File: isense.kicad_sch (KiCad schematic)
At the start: 29 parts, among them U2 OPA551U, U3 OPA551U, U4 TLV9301

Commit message: Update Mouser part numbers
Some resistors will be wrong, please check
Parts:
- U?: Mouser Part Number (none) -> 595-INA138NA/3K
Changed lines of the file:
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@@
+			)
+		)
+		(property "Mouser Part Number" "595-INA138NA/3K"
+			(at 44.45 41.91 0)
+			(effects
+				(font
+					(size 1.27 1.27)
+				)
+				(hide yes)
 			)
 		)

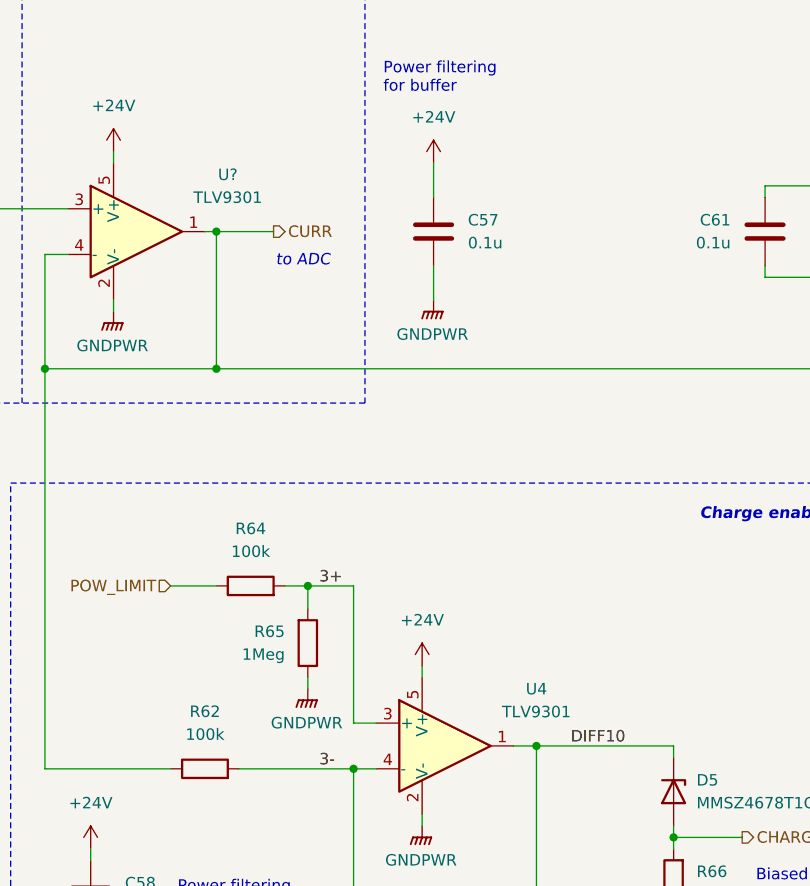
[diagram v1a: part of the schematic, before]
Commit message: Tuned circuits & adjusted values
Changed footprints for some circuits to consolidate components
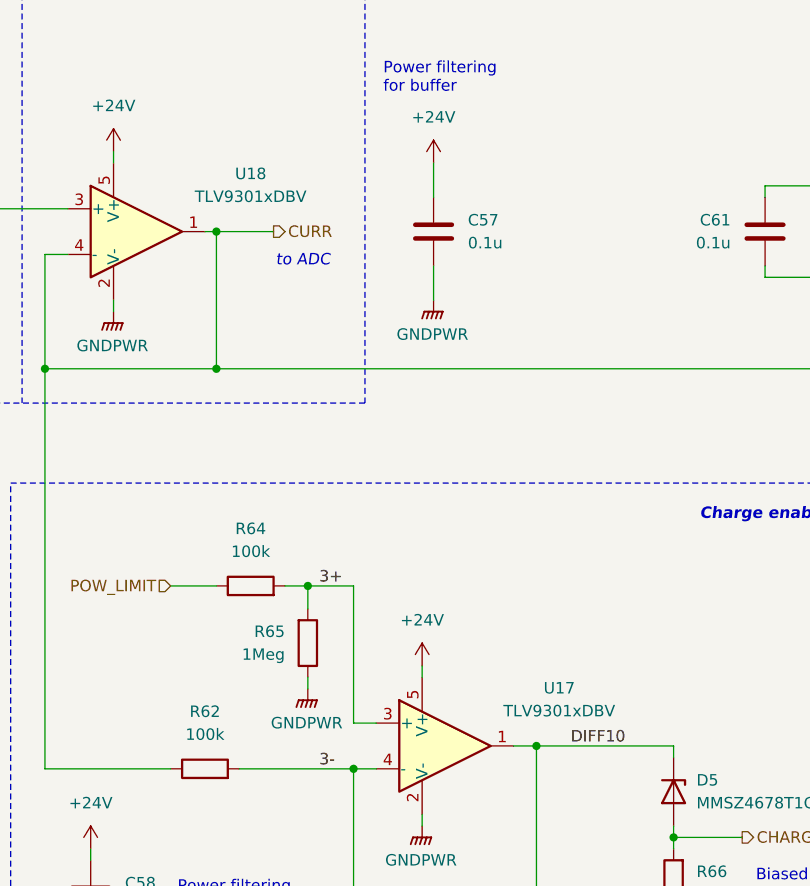
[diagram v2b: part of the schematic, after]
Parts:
- removed U4, U?: TLV9301, Package_TO_SOT_SMD:SOT-23-5_HandSoldering, symbol Amplifier_Operational:LM321
- added U17, U18: TLV9301xDBV, Package_TO_SOT_SMD:SOT-23-5_HandSoldering, symbol Amplifier_Operational:TLV9301xDBV
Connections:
- net +24V: now also U17.5 (V+), U18.5 (V+)
- net 3+: now also U17.3 (+)
- net 3-: now also U17.4 (-)
- net CURR: now also U18.1, U18.4 (-)
- net CURR_{RAW}: now also U18.3 (+)
- net DIFF10: now also U17.1
- net GNDPWR: now also U17.2 (V-), U18.2 (V-)

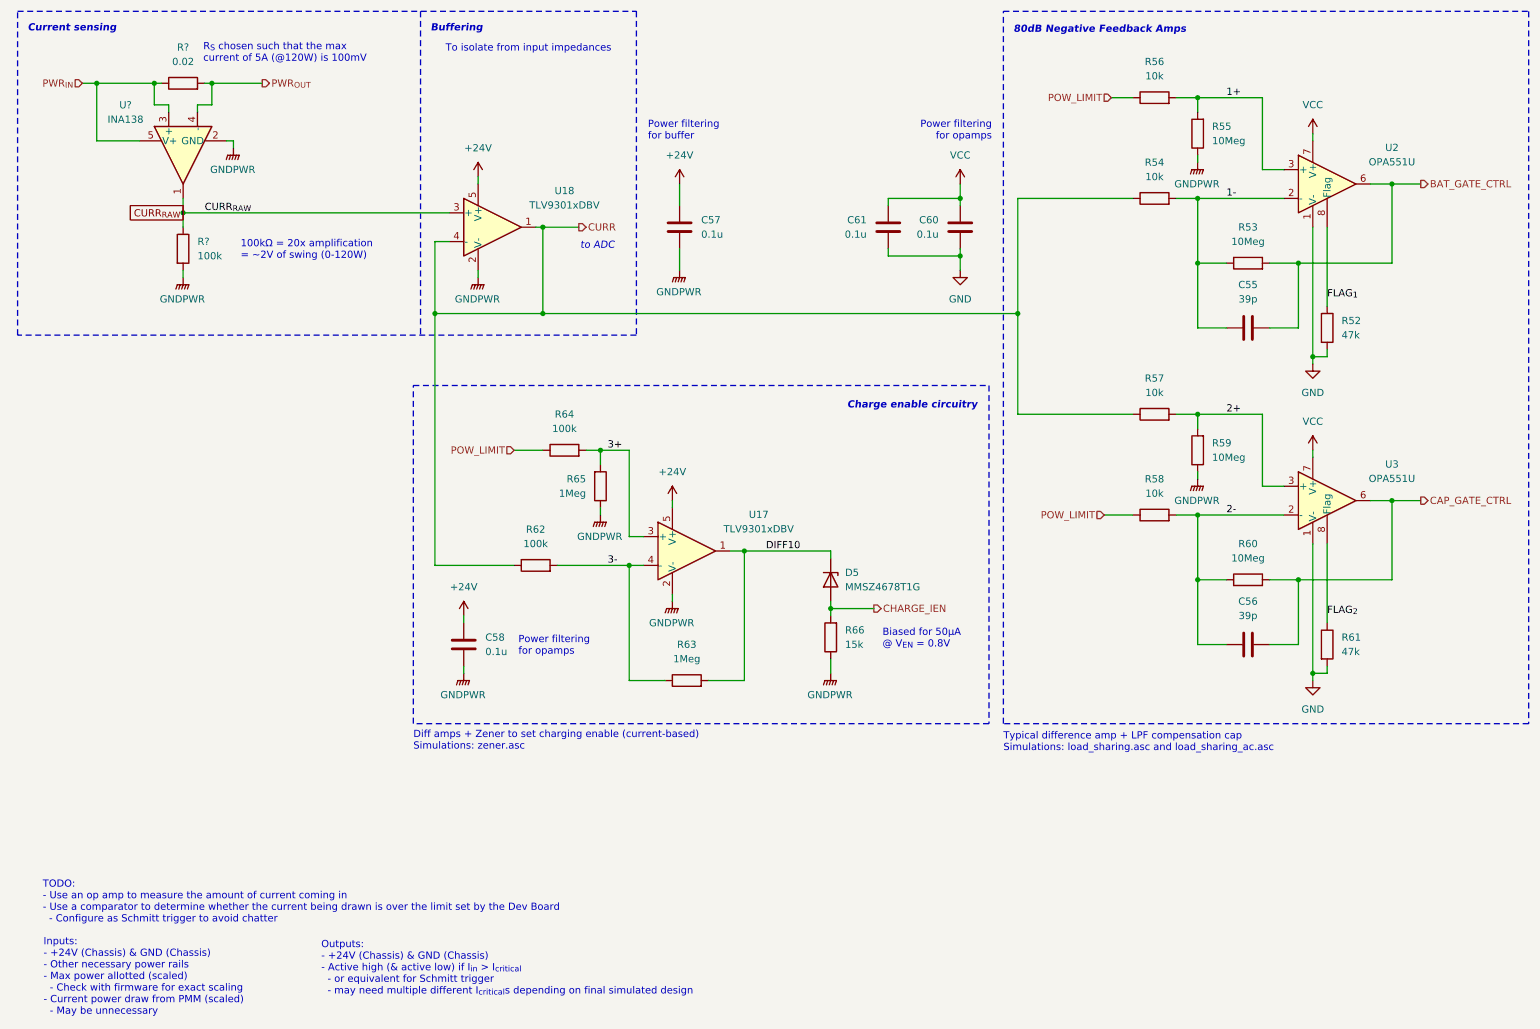
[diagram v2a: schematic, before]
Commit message: Transfer new design to schematic
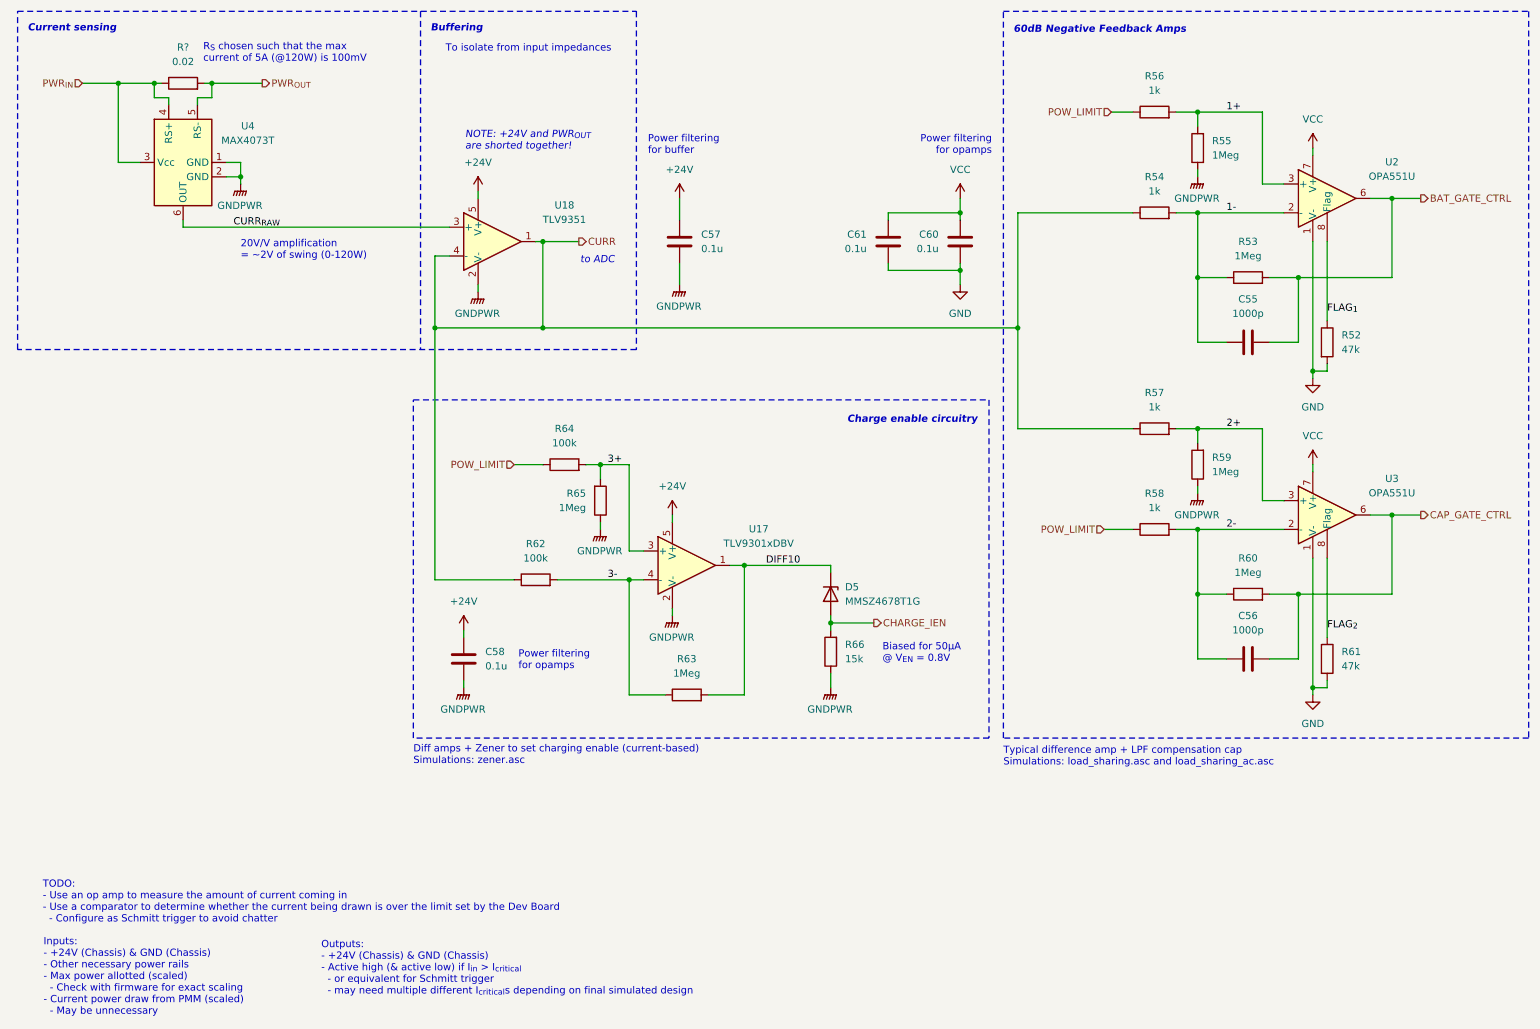
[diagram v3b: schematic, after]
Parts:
- removed R?: 100k, Resistor_SMD:R_0603_1608Metric_Pad0.98x0.95mm_HandSolder, symbol Device:R
- removed U?: INA138, Package_TO_SOT_SMD:SOT-23-5, symbol Amplifier_Current:INA138
- added U4: MAX4073T, Package_TO_SOT_SMD:SOT-23-6_Handsoldering, symbol Amplifier_Current:MAX4080T
- C55, C56: value 39p -> 1000p
- R53, R55, R59, R60: value 10Meg -> 1Meg
- R54, R56, R57, R58: value 10k -> 1k
- U18: value TLV9301xDBV -> TLV9351; Mouser Part Number 595-TLV9301IDBVR -> 595-TLV9351IDCKR
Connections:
- net CURR_{RAW}: now also U4.6 (OUT)
- net GNDPWR: now also U4.1 (GND), U4.2 (GND)
- net PWR_{IN}: now also U4.3 (Vcc), U4.4 (RS+)
- net PWR_{OUT}: now also U4.5 (RS-)
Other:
- note added: "20V/V amplification = ~2V of swing (0-120W)"
- note added: "60dB Negative Feedback Amps"
- note added: "NOTE: +24V and PWR_{OUT} are shorted together!"
- note removed: "100kΩ = 20x amplification = ~2V of swing (0-120W)"
- note removed: "80dB Negative Feedback Amps"
- moved on the sheet: C55, C56, C57, C58, C60, C61, D5, R52, R53, R54, R55, R56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

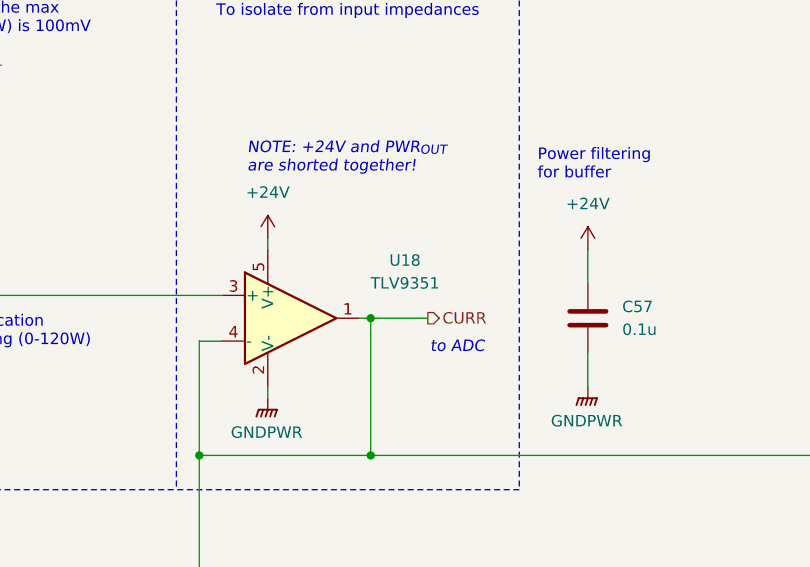
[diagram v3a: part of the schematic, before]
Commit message: Find suitable op-amp for buffer in current sense
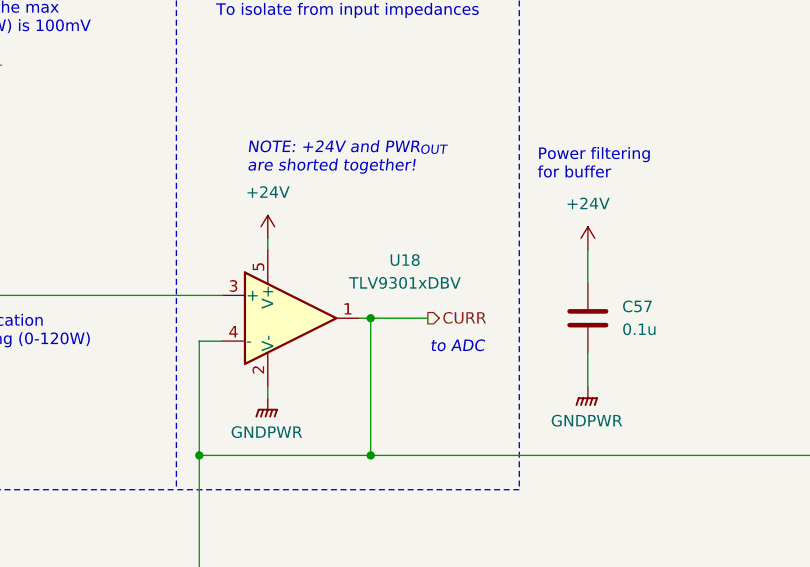
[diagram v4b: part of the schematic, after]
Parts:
- U18: value TLV9351 -> TLV9301xDBV; Mouser Part Number 595-TLV9351IDCKR -> 595-TLV9301IDBVR

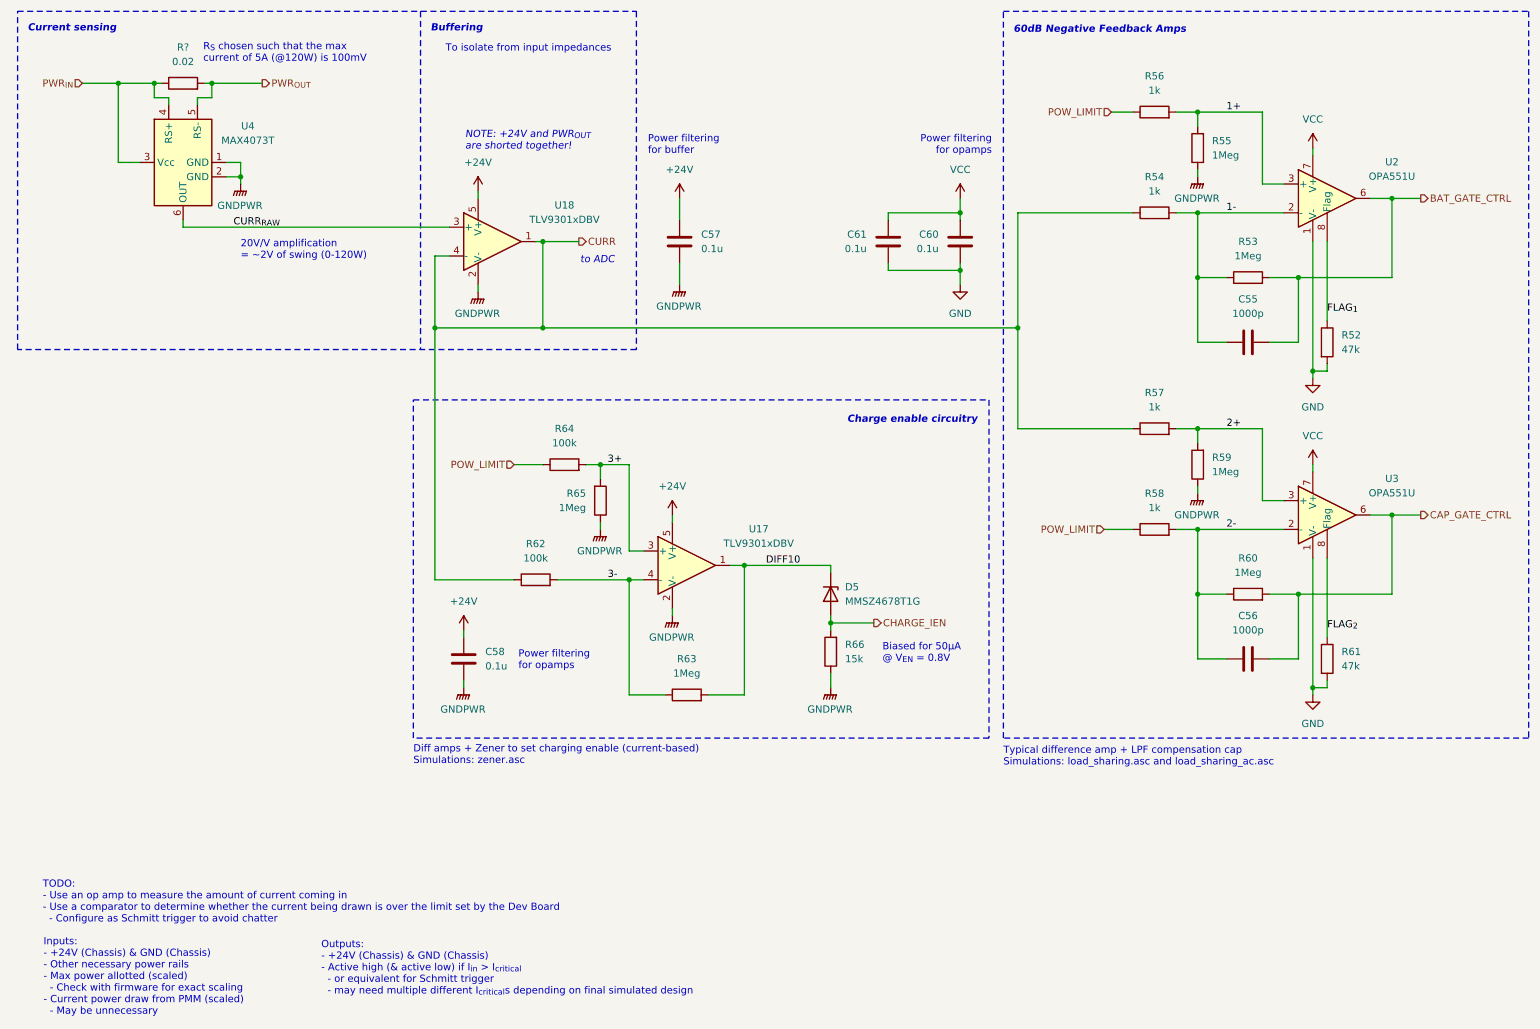
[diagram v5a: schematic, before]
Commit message: Reannotate schematic
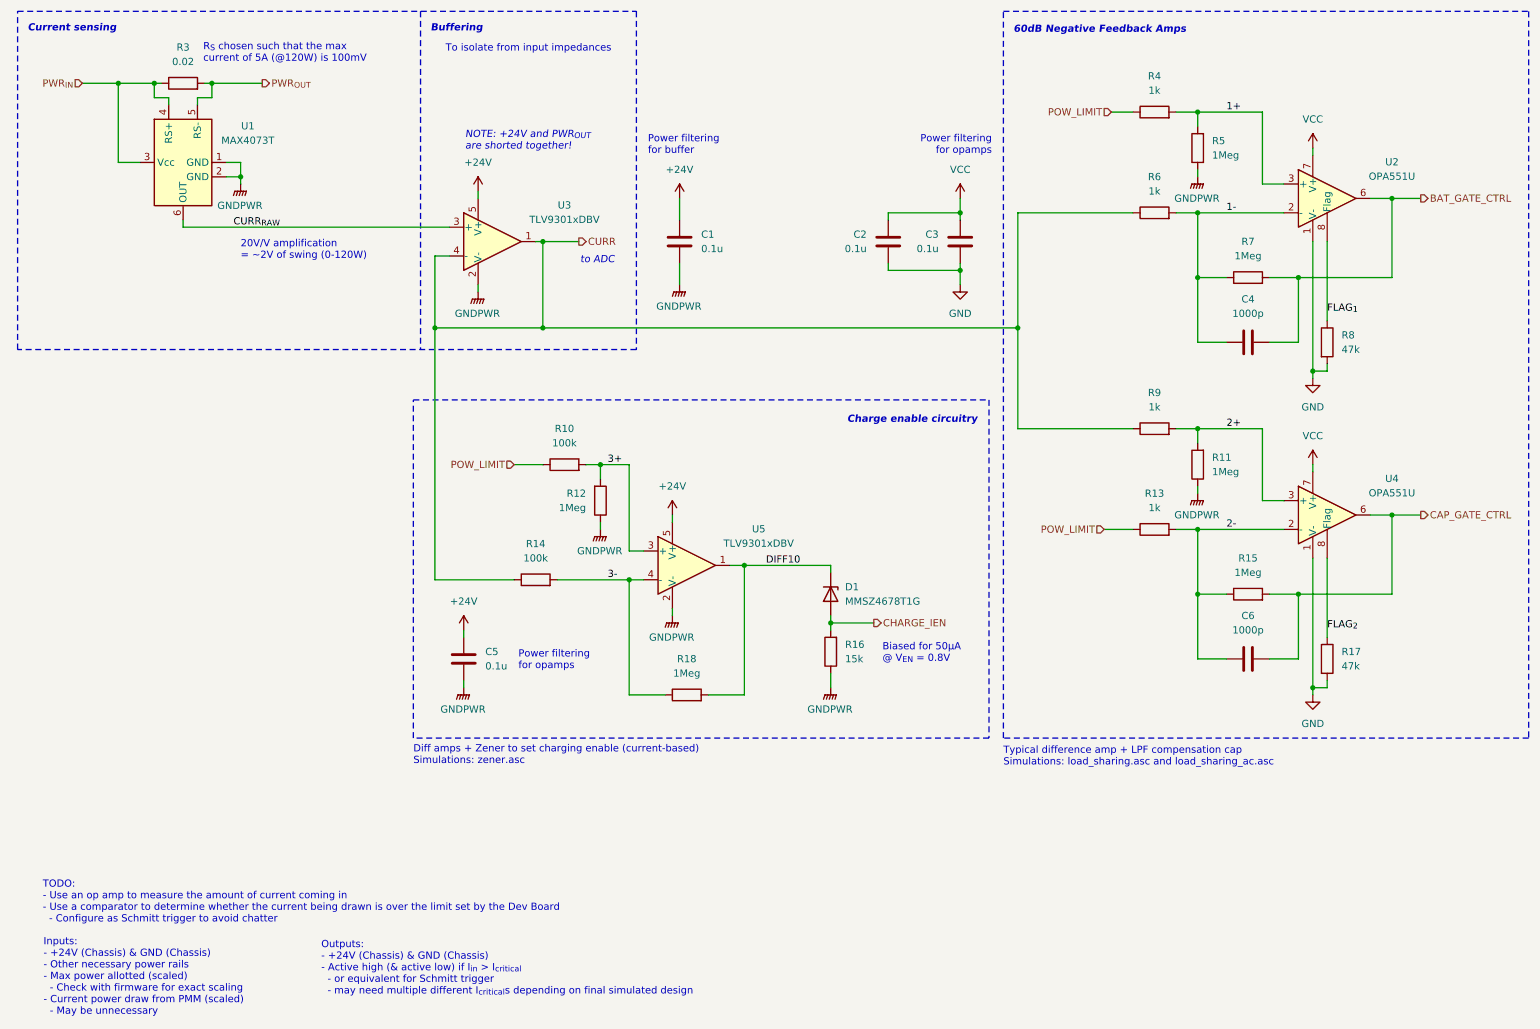
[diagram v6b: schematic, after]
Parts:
- gave numbers to parts that had none: 1
- renumbered C57 to C1, C61 to C2, C60 to C3, C55 to C4, C58 to C5, C56 to C6, D5 to D1, R64 to R10, R59 to R11, R65 to R12, R58 to R13, R62 to R14, R60 to R15, R66 to R16, R61 to R17, R63 to R18, R56 to R4, R55 to R5, R54 to R6, R53 to R7, R52 to R8, R57 to R9, U4 to U1, U18 to U3, U3 to U4, U17 to U5

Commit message: Adjusted some things + changed discharge to have a smaller time constant
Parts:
- R12, R18: Mouser Part Number (none) -> 603-RC0603FR-1010ML
- R13, R4, R6, R9: Mouser Part Number (none) -> 755-ESR03EZPJ222
- R16: Mouser Part Number (none) -> 603-RC0603FR-071M05L
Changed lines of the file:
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@@
 			)
 		)
+		(property "Mouser Part Number" "603-RC0603FR-071M05L"
+			(at 158.75 129.54 0)
+			(effects
+				(font
+					(size 1.27 1.27)
+				)
+				(hide yes)
+			)
+		)
 		(pin "1"
 		)
@@
 			)
 		)
-		(property "Datasheet" "~"
+		(property "Datasheet" "https://www.mouser.com/datasheet/2/447/PYu_RC_Group_51_RoHS_L_11-1984063.pdf"
 			(at 118.11 102.87 0)
 			(effects
@@
 			)
 		)
+		(property "Mouser Part Number" "603-RC0603FR-1010ML"
+			(at 118.11 102.87 0)
+			(effects
+				(font
+					(size 1.27 1.27)
+				)
+				(hide yes)
+			)
+		)
 		(pin "1"
 		)
@@
 			)
 		)
-		(property "Datasheet" "~"
+		(property "Datasheet" "https://www.rohm.com/datasheet?p=ESR03EZPJ&dist=Mouser&media=referral&source=mouser.com&campaign=Mouser"
 			(at 215.9 52.07 0)
 			(effects
@@
 			)
 		)
+		(property "Mouser Part Number" "755-ESR03EZPJ222"
+			(at 215.9 52.07 0)
+			(effects
+				(font
+					(size 1.27 1.27)
+				)
+				(hide yes)
+			)
+		)
 		(pin "1"
 		)
@@
 			)
 		)
-		(property "Datasheet" "~"
+		(property "Datasheet" "https://www.rohm.com/datasheet?p=ESR03EZPJ&dist=Mouser&media=referral&source=mouser.com&campaign=Mouser"
 			(at 215.9 107.95 0)
 			(effects
@@
 			)
 		)
+		(property "Mouser Part Number" "755-ESR03EZPJ222"
+			(at 215.9 107.95 0)
+			(effects
+				(font
+					(size 1.27 1.27)
+				)
+				(hide yes)
+			)
+		)
 		(pin "1"
 		)
@@
 			)
 		)
-		(property "Datasheet" "~"
+		(property "Datasheet" "https://www.mouser.com/datasheet/2/447/PYu_RC_Group_51_RoHS_L_11-1984063.pdf"
 			(at 133.35 137.16 0)
 			(effects
@@
 			)
 		)
+		(property "Mouser Part Number" "603-RC0603FR-1010ML"
+			(at 133.35 137.16 0)
+			(effects
+				(font
+					(size 1.27 1.27)
+				)
+				(hide yes)
+			)
+		)
 		(pin "1"
 		)
@@
 			)
 		)
-		(property "Datasheet" "~"
+		(property "Datasheet" "https://www.rohm.com/datasheet?p=ESR03EZPJ&dist=Mouser&media=referral&source=mouser.com&campaign=Mouser"
 			(at 215.9 90.17 0)
 			(effects
@@
 			)
 		)
+		(property "Mouser Part Number" "755-ESR03EZPJ222"
+			(at 215.9 90.17 0)
+			(effects
+				(font
+					(size 1.27 1.27)
+				)
+				(hide yes)
+			)
+		)
 		(pin "1"
 		)
@@
 			)
 		)
-		(property "Datasheet" "~"
+		(property "Datasheet" "https://www.rohm.com/datasheet?p=ESR03EZPJ&dist=Mouser&media=referral&source=mouser.com&campaign=Mouser"
 			(at 215.9 34.29 0)
 			(effects
@@
 			)
 		)
+		(property "Mouser Part Number" "755-ESR03EZPJ222"
+			(at 215.9 34.29 0)
+			(effects
+				(font
+					(size 1.27 1.27)
+				)
+				(hide yes)
+			)
+		)
